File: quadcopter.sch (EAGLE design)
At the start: 65 parts, among them J1 ISP, U1 ATMEGA128RFA1

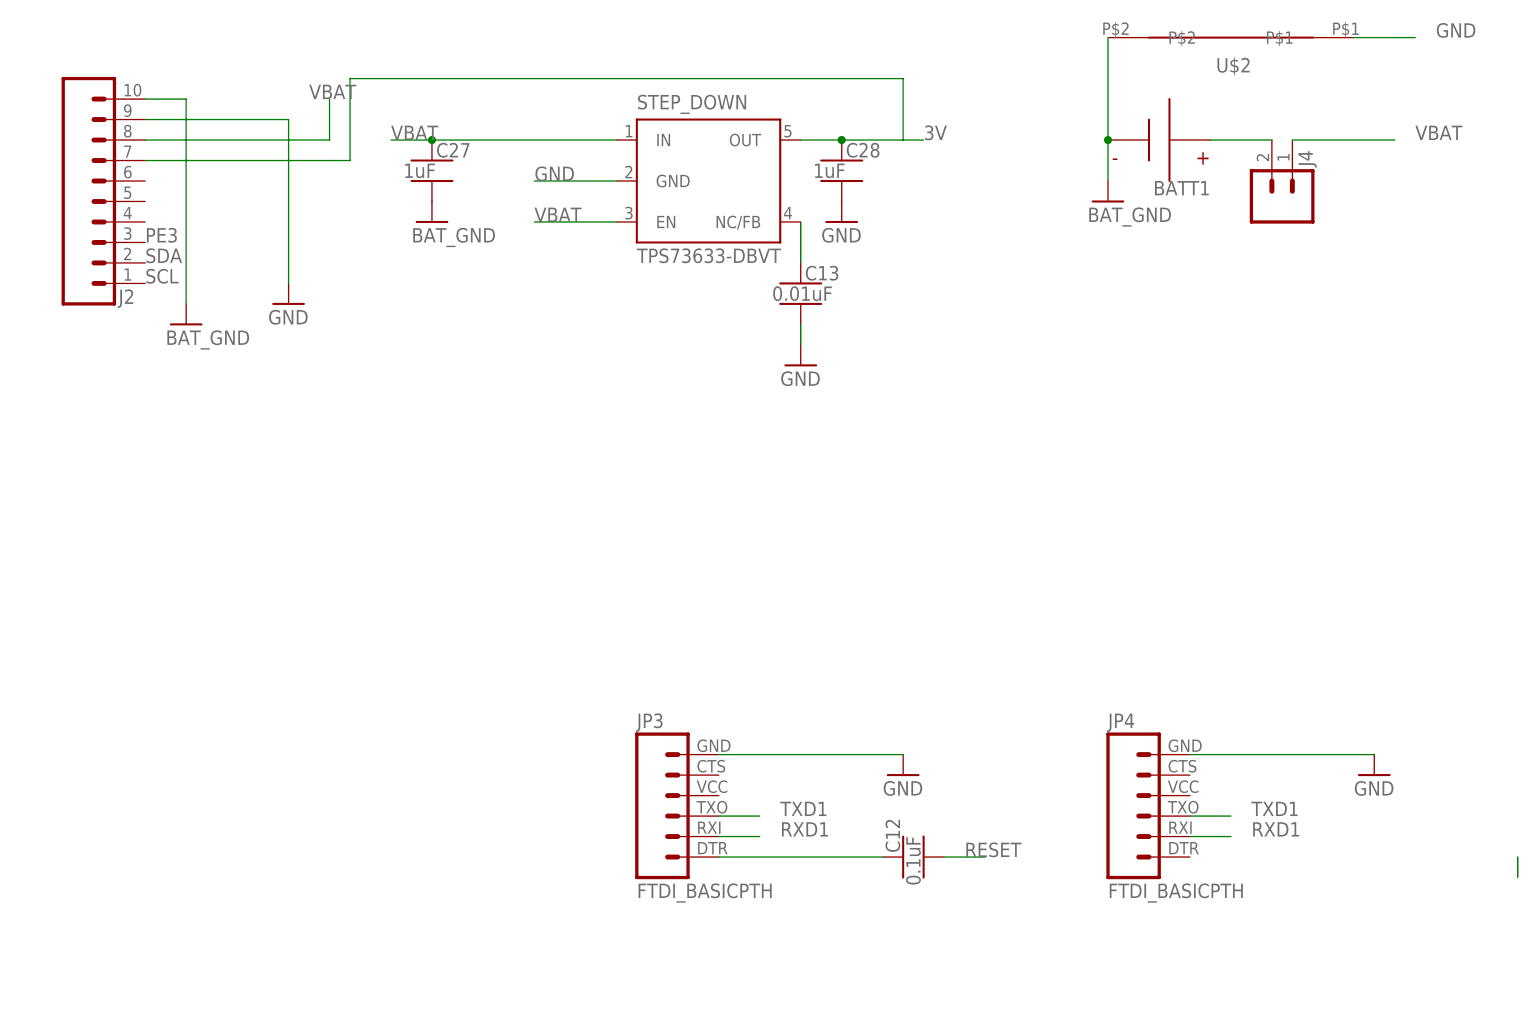
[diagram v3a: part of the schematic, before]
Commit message: There surely are a ton of mistakes, but I'm not sure what they are. I had to do a ton of routing by hand
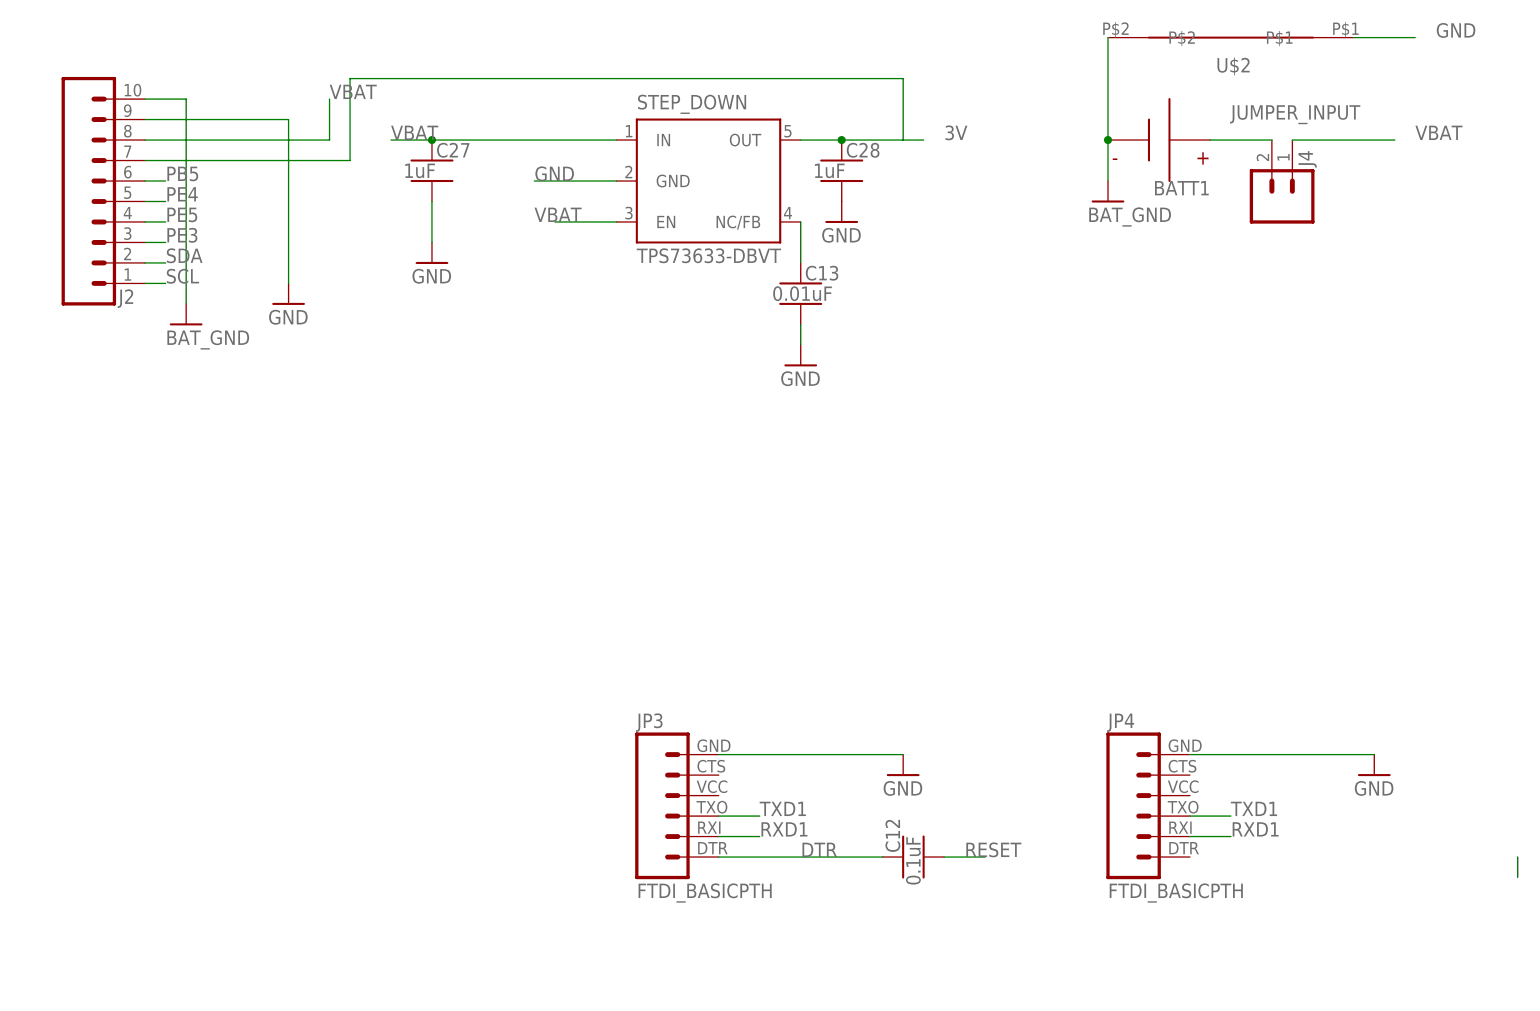
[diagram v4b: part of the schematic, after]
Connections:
- net N$1 renamed JUMPER_INPUT
- net N$9 renamed DTR
- removed net N$21: C27.1, STEP_DOWN.IN
- removed net N$22: STEP_DOWN.GND
- removed net N$27: STEP_DOWN.EN
- removed net N$8: JP3.6, JP4.6
- net BAT_GND: no longer C27.2
- net GND: now also C27.2, JP3.6, JP4.6, STEP_DOWN.GND
- net PB5: now also J2.6
- net PE3: now also J2.3
- net PE4: now also J2.5
- net PE5: now also J2.4
- net SCL: now also J2.1
- net SDA: now also J2.2
- net VBAT: now also C27.1, STEP_DOWN.EN, STEP_DOWN.IN

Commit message: routed and everything
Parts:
- removed C23, C25, C29, C33: 100uf, capacitor-wima:C10/4
- removed R15, R16, R20, R22: 100R, Lab5:R-US_R0805
- added C14, C19, C20, C9: 220uF, quadparts_prebuilt:CAPACITOR-POL_SMD-7043-D_TANTALUM-220UF
- added R4, R5, R6, R9: 100, quadparts_prebuilt:RESISTOR_SMD-2012-0805-100
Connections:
- removed net CLKI: U1.CLKI
- removed net N$17: U$1.P$6.SDO_M, U$1.P$7.CS_A/G, U$1.P$8.CS_M
- removed net N$23: U1.DEVDD, U1.EVDD
- removed net N$24: R1.2
- removed net N$25: C4.1
- removed net N$26: C3.1
- removed net TST: U1.TST
- net 3V: now also C3.1, C4.1, R1.2, U$1.P$6.SDO_M, U$1.P$7.CS_A/G, U$1.P$8.CS_M, U1.DEVDD, U1.EVDD
- net BAT_GND: now also C10.2, C14.-, C19.-, C20.-, C24.2, C27.2, C30.2, C34.2, C9.-, R10.1, R17.1, R21.1, R23.1, U$16.S, U$18.S, U$20.S, U$7.S
- net FILTERED: now also R5.2; no longer R16.2
- net FILTERED1: now also R6.2; no longer R20.2
- net FILTERED3: now also R4.2; no longer R15.2
- net FILTERED5: now also R9.2; no longer R22.2
- net GND: now also U1.CLKI, U1.TST; no longer C10.2, C23.2, C24.2, C25.2, C27.2, C29.2, C30.2, C33.2, C34.2, R10.1, R17.1, R21.1, R23.1, U$16.S, U$18.S, U$20.S, U$7.S
- net PB5: now also R5.1; no longer R16.1
- net PE3: now also R4.1; no longer R15.1
- net PE4: now also R6.1; no longer R20.1
- net PE5: now also R9.1; no longer R22.1
- net RX1: now also JP4.3
- net RXD1: now also JP3.3; no longer JP3.2, JP4.2
- net TX1: now also JP4.2
- net TXD1: now also JP3.2; no longer JP3.3, JP4.3
- net VBAT: now also C14.+, C19.+, C20.+, C9.+; no longer C23.1, C25.1, C29.1, C33.1
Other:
- note removed: "Design review said SDO_M should be set low, but talked with person with advice from prof, and prof said set high. This sets less significant bit, not necessarily the least sig bit"
- note removed: "SDO_A/G should be set high to enable I2C"

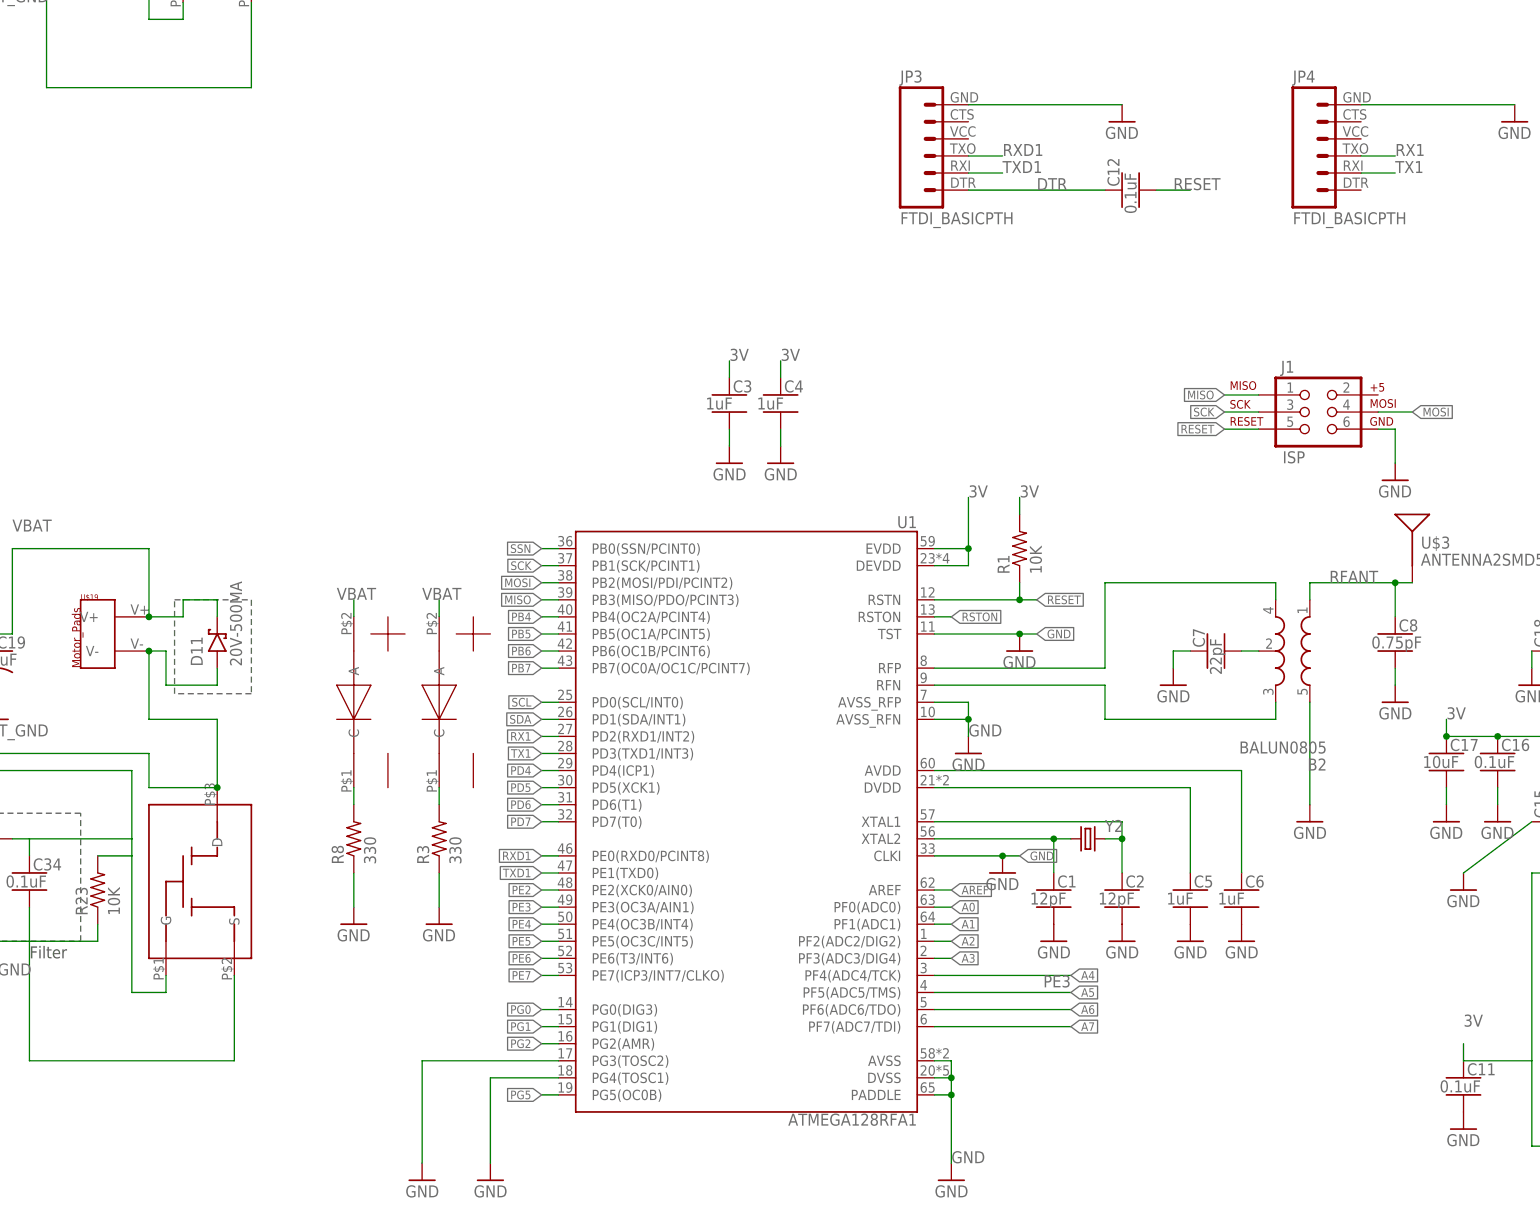
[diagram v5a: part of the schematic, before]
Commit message: worked on routing more, there are still lots of drc issues though
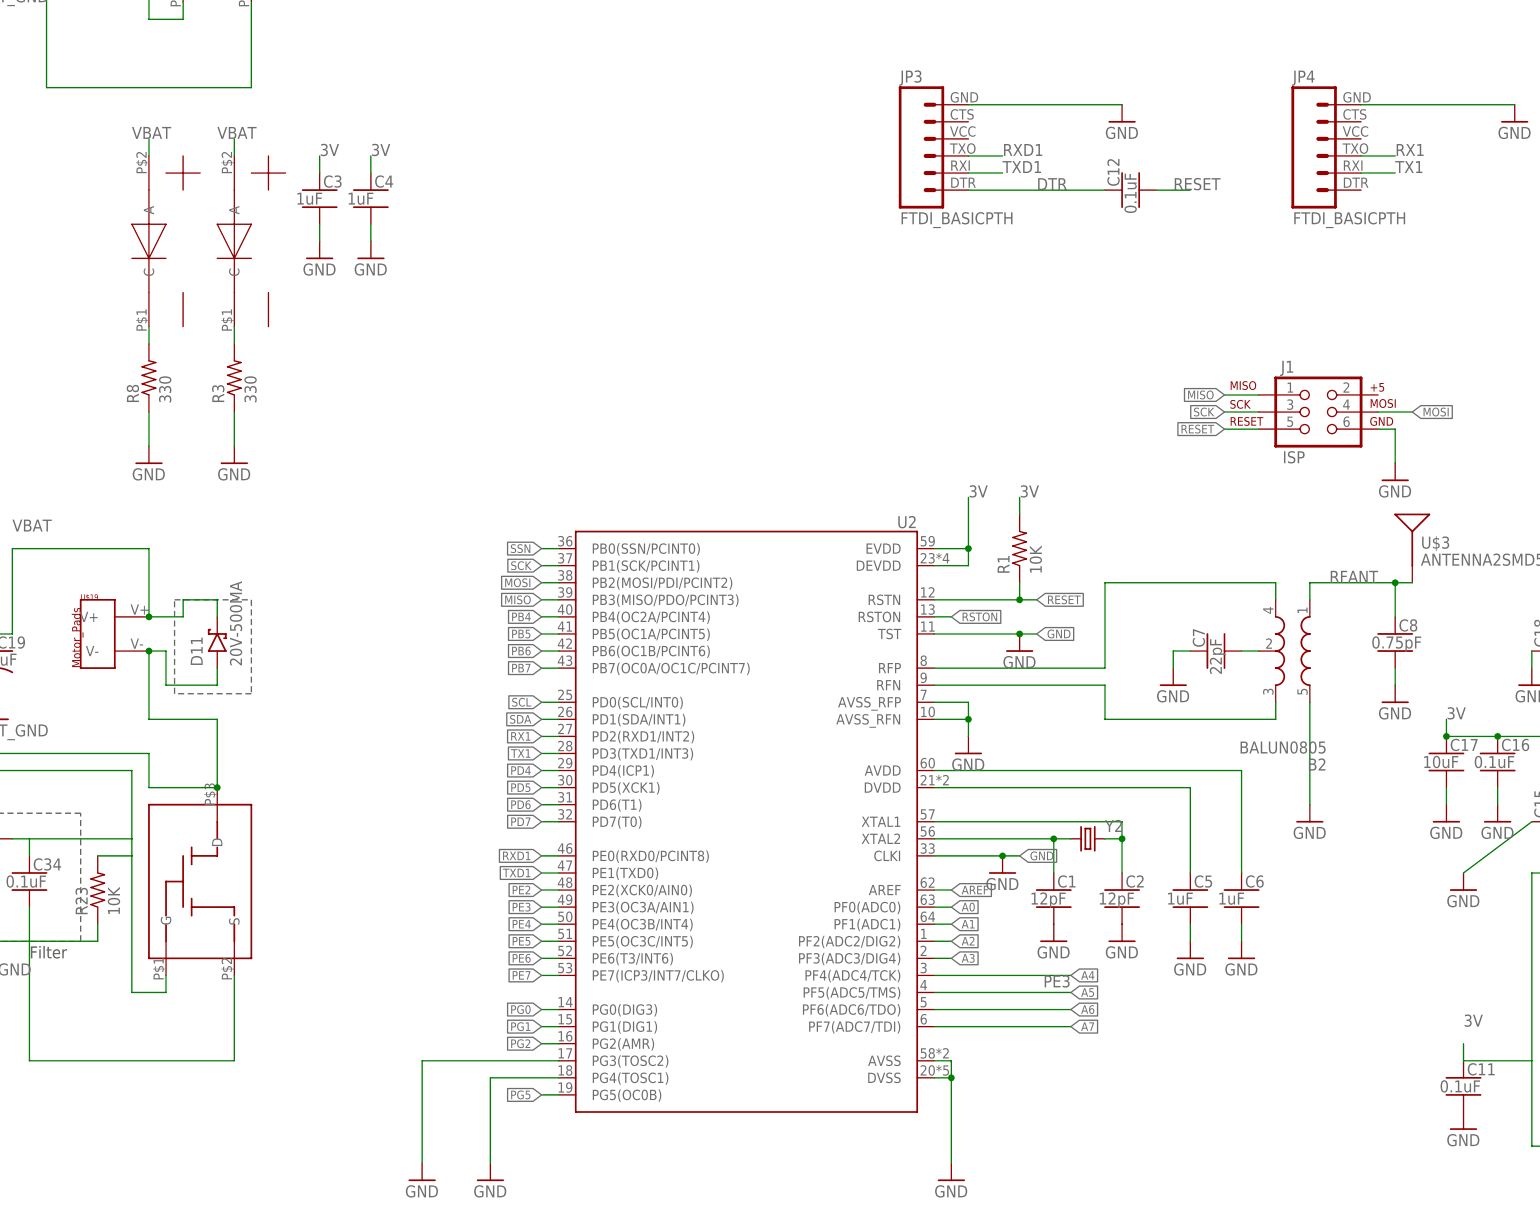
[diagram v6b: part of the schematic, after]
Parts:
- removed U1: ATMEGA128RFA1, SparkFun-DigitalIC:ATMEGA128RFA1
- added U2: ATMEGA128RFA1, quadparts_prebuilt:ATMEGA128RFA1
- J1: device SparkFun-Connectors:AVR_SPI_PRG_6NS -> quadparts_prebuilt:AVR_SPI_PRG_6NS
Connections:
- net 3V: now also U2.DEVDD, U2.EVDD; no longer U1.DEVDD, U1.EVDD
- net A0: now also U2.PF0(ADC0); no longer U1.PF0(ADC0)
- net A1: now also U2.PF1(ADC1); no longer U1.PF1(ADC1)
- net A2: now also U2.PF2(ADC2/DIG2); no longer U1.PF2(ADC2/DIG2)
- net A3: now also U2.PF3(ADC3/DIG4); no longer U1.PF3(ADC3/DIG4)
- net A4: now also U2.PF4(ADC4/TCK); no longer U1.PF4(ADC4/TCK)
- net A5: now also U2.PF5(ADC5/TMS); no longer U1.PF5(ADC5/TMS)
- net A6: now also U2.PF6(ADC6/TDO); no longer U1.PF6(ADC6/TDO)
- net A7: now also U2.PF7(ADC7/TDI); no longer U1.PF7(ADC7/TDI)
- net AREF: now also U2.AREF; no longer U1.AREF
- net AVDD: now also U2.AVDD; no longer U1.AVDD
- net DVDD: now also U2.DVDD; no longer U1.DVDD
- net GND: now also U2.AVSS, U2.AVSS_RFN, U2.AVSS_RFP, U2.CLKI, U2.DVSS, U2.PG3(TOSC2), U2.PG4(TOSC1), U2.TST; no longer U1.AVSS, U1.AVSS_RFN, U1.AVSS_RFP, U1.CLKI, U1.DVSS, U1.PADDLE, U1.PG3(TOSC2), U1.PG4(TOSC1), U1.TST
- net MISO: now also U2.PB3(MISO/PDO/PCINT3); no longer U1.PB3(MISO/PDO/PCINT3)
- net MOSI: now also U2.PB2(MOSI/PDI/PCINT2); no longer U1.PB2(MOSI/PDI/PCINT2)
- net N$3: now also U2.XTAL1; no longer U1.XTAL1
- net N$4: now also U2.XTAL2; no longer U1.XTAL2
- net PB4: now also U2.PB4(OC2A/PCINT4); no longer U1.PB4(OC2A/PCINT4)
- net PB5: now also U2.PB5(OC1A/PCINT5); no longer U1.PB5(OC1A/PCINT5)
- net PB6: now also U2.PB6(OC1B/PCINT6); no longer U1.PB6(OC1B/PCINT6)
- net PB7: now also U2.PB7(OC0A/OC1C/PCINT7); no longer U1.PB7(OC0A/OC1C/PCINT7)
- net PD4: now also U2.PD4(ICP1); no longer U1.PD4(ICP1)
- net PD5: now also U2.PD5(XCK1); no longer U1.PD5(XCK1)
- net PD6: now also U2.PD6(T1); no longer U1.PD6(T1)
- net PD7: now also U2.PD7(T0); no longer U1.PD7(T0)
- net PE2: now also U2.PE2(XCK0/AIN0); no longer U1.PE2(XCK0/AIN0)
- net PE3: now also U2.PE3(OC3A/AIN1); no longer U1.PE3(OC3A/AIN1)
- net PE4: now also U2.PE4(OC3B/INT4); no longer U1.PE4(OC3B/INT4)
- net PE5: now also U2.PE5(OC3C/INT5); no longer U1.PE5(OC3C/INT5)
- net PE6: now also U2.PE6(T3/INT6); no longer U1.PE6(T3/INT6)
- net PE7: now also U2.PE7(ICP3/INT7/CLKO); no longer U1.PE7(ICP3/INT7/CLKO)
- net PG0: now also U2.PG0(DIG3); no longer U1.PG0(DIG3)
- net PG1: now also U2.PG1(DIG1); no longer U1.PG1(DIG1)
- net PG2: now also U2.PG2(AMR); no longer U1.PG2(AMR)
- net PG5: now also U2.PG5(OC0B); no longer U1.PG5(OC0B)
- net RESET: now also U2.RSTN; no longer U1.RSTN
- net RFN: now also U2.RFN; no longer U1.RFN
- net RFP: now also U2.RFP; no longer U1.RFP
- net RSTON: now also U2.RSTON; no longer U1.RSTON
- net RX1: now also U2.PD2(RXD1/INT2); no longer U1.PD2(RXD1/INT2)
- net RXD1: now also U2.PE0(RXD0/PCINT8); no longer U1.PE0(RXD0/PCINT8)
- net SCK: now also U2.PB1(SCK/PCINT1); no longer U1.PB1(SCK/PCINT1)
- net SCL: now also U2.PD0(SCL/INT0); no longer U1.PD0(SCL/INT0)
- net SDA: now also U2.PD1(SDA/INT1); no longer U1.PD1(SDA/INT1)
- net SSN: now also U2.PB0(SSN/PCINT0); no longer U1.PB0(SSN/PCINT0)
- net TX1: now also U2.PD3(TXD1/INT3); no longer U1.PD3(TXD1/INT3)
- net TXD1: now also U2.PE1(TXD0); no longer U1.PE1(TXD0)
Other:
- moved on the sheet: C3, C4, R3, R8
